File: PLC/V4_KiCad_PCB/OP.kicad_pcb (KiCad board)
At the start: 2 copper layers, 208 x 80 mm, 307 parts, among them J1 MSTBVA-2.5-10-5.08, J10 01x03_fem, J11 01x02_fem, J12 01x15_fem, J13 01x03_fem, J14 01x15_fem, J15 01x04_fem, J16 MSTBVA-2.5-10-5.08, J17 MSTBVA-2.5-10-5.08, J2 MSTBVA-2.5-10-5.08, J25 01x05_fem, J27 Lötauge, J28 GND_CAN opt an J33, J3 PFS 2x4, J33 opt. GND_XXX, J37 Lötauge, J4 01x08_fem, J40 Extention, J41 Lötauge, J42 Lötauge, J43 Flachstecker, J44 Lötauge, J45 Lötauge, J46 Lötauge, J47 Lötauge, J48 Lötauge, J5 01x04_fem, J51 Lötauge, J52 Lötauge, J6 DIN-5, J61 Lötauge, J62 Lötauge, J7 DIN-5, J8 02x02_fem, J9 Ub 0V PE, P1 1,0K lin, P2 1,0K lin, Q1 IRLML 2244, SW1 SW_DIP_x02, SW2 SW_DIP_x02, SW3 SW_DIP_x02, U1 LTV-844, U10 ADM2483xRW, U2 LTV-844, U3 LTV-844, U36 MCP3204, U39 ADuM1401xRW, U4 LTV-844, U40 ADM-803R, U42 LM4040 AIM3-2.5, U43 LM4040 AIM3-2.5, U47 ADM-809Z, U48 ADM-803L, U49 74AHC1G32, U5 MCP23S17, U50 NE555DRG4, U6 ISO1050, U7 Teensy4.0, U8 ISO1050, U9 25LC512

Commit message: OP routing optimized
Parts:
- R163, R165: moved to F.Cu
- moved R163 22.2 mm to (86.6, 76.6), turned to 0 degrees
- moved R165 19.3 mm to (86.6, 78.3), turned to 0 degrees
- moved C10 1.98 mm to (89.6, 78.0)
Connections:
- D44 pad 2: Net-(D44-Pad2) -> /RS485_B
- D45 pad 1: Net-(D44-Pad2) -> /RS485_B
- D46 pad 2: Net-(D46-Pad2) -> /RS485_A
- D47 pad 1: Net-(D46-Pad2) -> /RS485_A
- R163 pad 2: Net-(D46-Pad2) -> Net-(R163-Pad2)
- R165 pad 2: Net-(D44-Pad2) -> Net-(R165-Pad2)
- U10 pad 12: Net-(D46-Pad2) -> Net-(R163-Pad2)
- U10 pad 13: Net-(D44-Pad2) -> Net-(R165-Pad2)
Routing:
- net Net-(D44-Pad2): track 36.7 -> 0.00 mm, vias 3 -> 0
- net Net-(D46-Pad2): track 31.8 -> 0.00 mm, vias 1 -> 0
- net /RS485_B: track 29.5 -> 59.9 mm, vias 3 -> 4
- net /RS485_A: track 34.1 -> 61.2 mm, vias 2 -> 3
- net Net-(R165-Pad2): track 0.00 -> 2.94 mm
- net Net-(R163-Pad2): track 0.00 -> 2.78 mm
- net /GND_RS485_BUS: track 66.5 -> 65.9 mm
- net GNDD: vias 152 -> 157

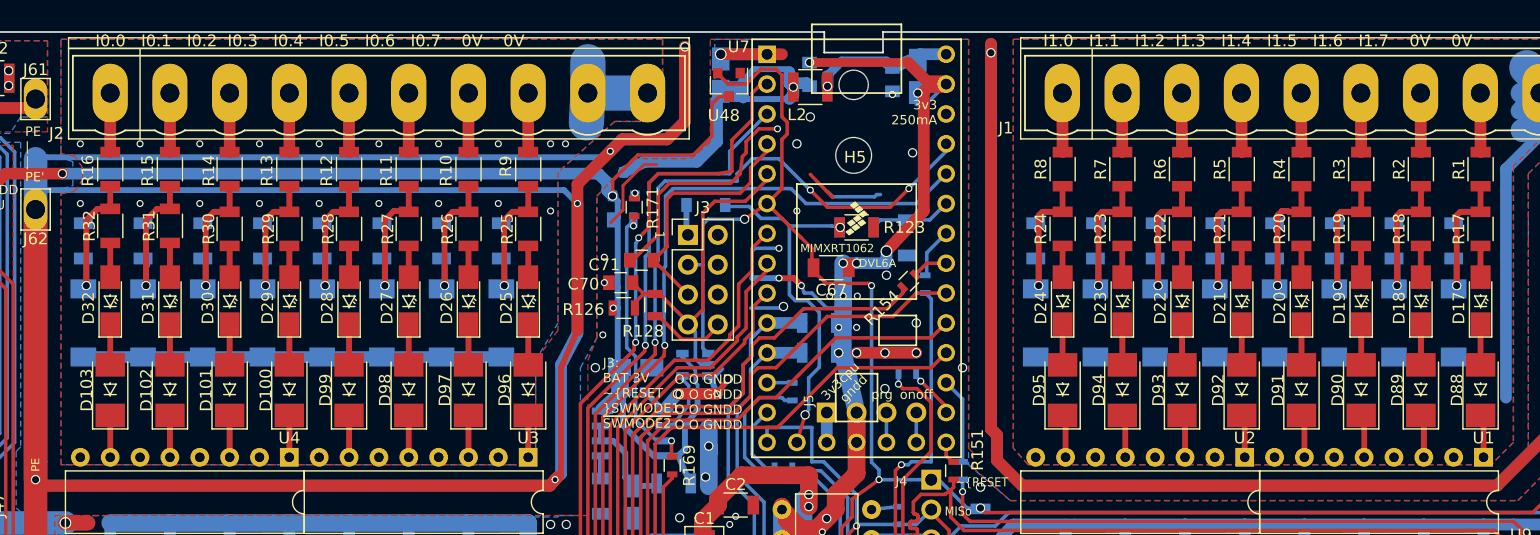
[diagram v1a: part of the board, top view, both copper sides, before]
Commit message: OP PCB mods CPU
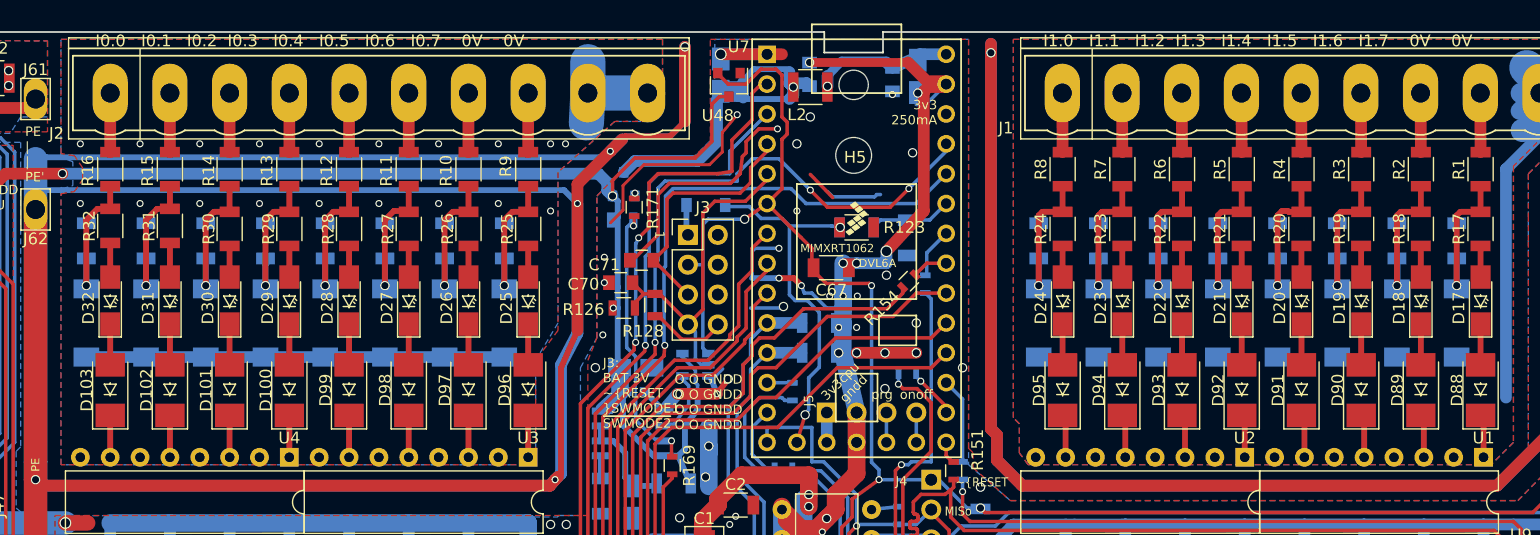
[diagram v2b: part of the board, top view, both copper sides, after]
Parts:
- moved C53 0.25 mm to (222.6, 57.8)
- moved C55 0.25 mm to (212.5, 57.8)
- moved C57 0.25 mm to (202.3, 57.8)
- moved C60 0.25 mm to (146.7, 57.8)
- moved C62 0.25 mm to (136.5, 57.8)
- moved D10 0.25 mm to (146.7, 64.8)
- moved D12 0.25 mm to (136.5, 64.8)
- moved D2 0.25 mm to (227.7, 64.8)
- moved D7 0.25 mm to (202.3, 64.8)
- moved C64 0.25 mm to (126.4, 57.8)
- moved C65 0.25 mm to (121.3, 57.8)
- moved C66 0.25 mm to (116.2, 57.8)
- moved D14 0.25 mm to (126.4, 64.8)
- moved D15 0.25 mm to (121.3, 64.8)
- moved D16 0.25 mm to (116.2, 64.8)
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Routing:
- net GNDD: track 689.0 -> 698.6 mm, vias 157 -> 158

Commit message: Kaltstart Überarbeitung
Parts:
- removed R50: 10k, Resistors_SMD:R_1206
- removed U40: ADM-803R, TO_SOT_Packages_SMD:SOT-23
- added C99: 100n, Capacitors_SMD:C_1206, F.Cu at (243.5, 76.6)
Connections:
- net /5V_CPU renamed Net-(C50-Pad1)
- net /COLDSTART_3V3INT renamed /3V3EN_Q2_UP
- C24 pad 2: /3V3_INTERFACE -> /3V3_INT
- C4 pad 1: /3V3_INTERFACE -> /3V3_INT
- C7 pad 2: /3V3_INTERFACE -> /3V3_INT
- C8 pad 1: /3V3_INTERFACE -> /3V3_INT
- D41 pad 2: /3V3_INTERFACE -> /3V3_INT
- J25 pad 1: /3V3_INTERFACE -> /3V3_INT
- J51 pad 1: /3V3_INTERFACE -> /3V3_INT
- R118 pad 2: /3V3_INTERFACE -> /3V3_INT
- U10 pad 1: /3V3_INTERFACE -> /3V3_INT
- U39 pad 1: /3V3_INTERFACE -> /3V3_INT
- U47 pad 3: /3V3_INTERFACE -> /3V3_INT
- U6 pad 1: /3V3_INTERFACE -> /3V3_INT
- U8 pad 1: /3V3_INTERFACE -> /3V3_INT
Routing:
- net /3V3_INTERFACE: track 154.1 -> 0.00 mm, vias 10 -> 0
- net /3V3_INT: track 217.4 -> 370.6 mm, vias 7 -> 17
- net GNDD: track 698.6 -> 696.9 mm, vias 158 -> 160

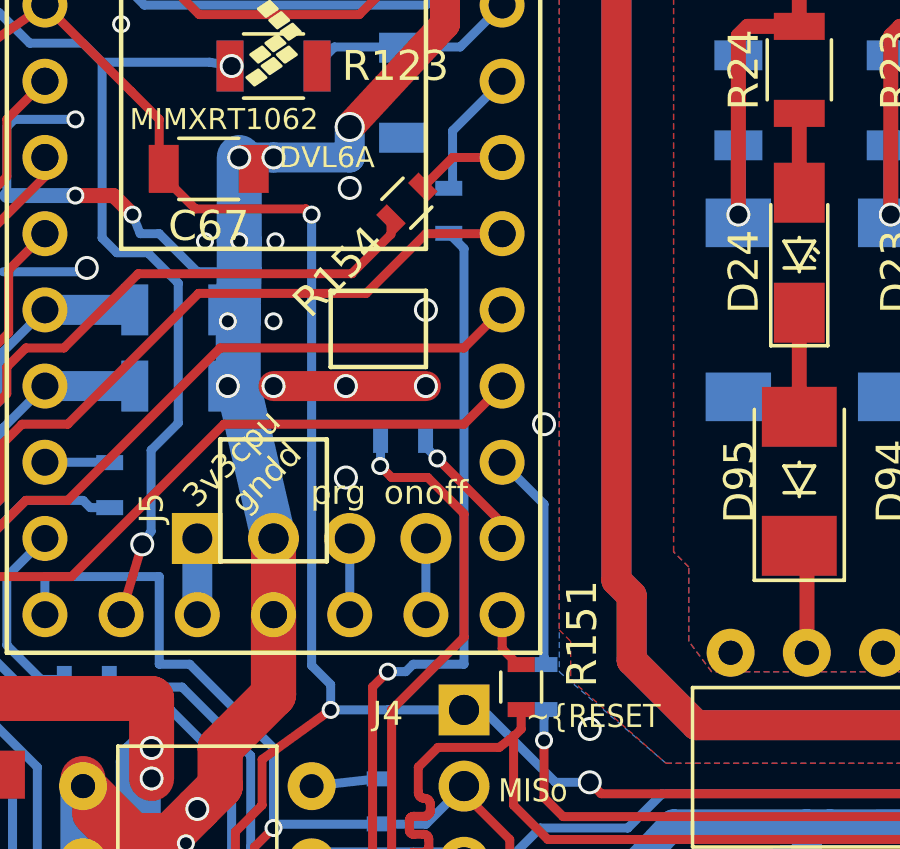
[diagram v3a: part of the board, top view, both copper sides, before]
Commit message: Überarbeitung 4-Layer-Layout und Dokumentation
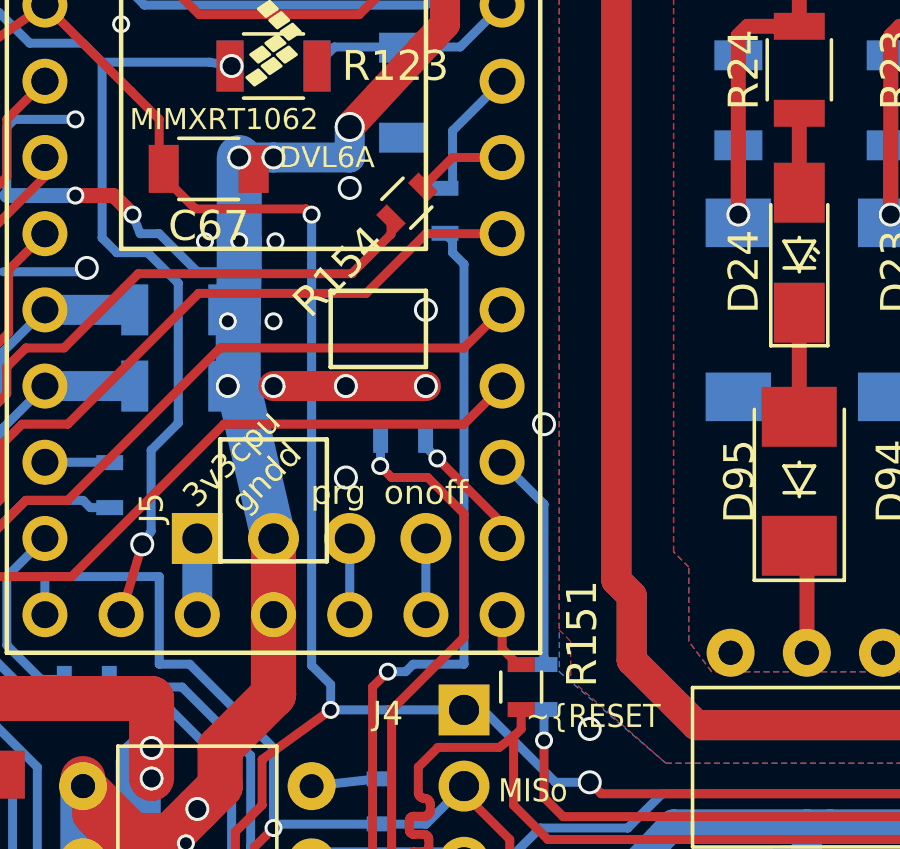
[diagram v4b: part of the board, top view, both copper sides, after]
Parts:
- moved R155 0.13 mm to (187.5, 61.5)

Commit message: V2.6 R38 final PFS
M38 final Version for PFS variant
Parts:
- added R501: 10k, Resistors_SMD:R_1206, F.Cu at (245.0, 76.7)
- moved C99 0.83 mm to (242.7, 76.6)
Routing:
- net GNDD: track 696.9 -> 692.7 mm
- net /PE: track 1070.4 -> 1068.7 mm
- net /~EE_HOLD: vias 3 -> 2
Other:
- board text added: "PE PE 3V3 (7) (11) ~RES ~CS SO CK SI GNDD"
- board text added: "PFS CPU Board V2.6 M38 2024-01-17"
- board text removed: "PE PE 3V3 (7) GNDD (11) ~RES ~CS SO CK SI GNDD"
- board text removed: "PFS CPU Board V2.6 M37 2023-11-23"

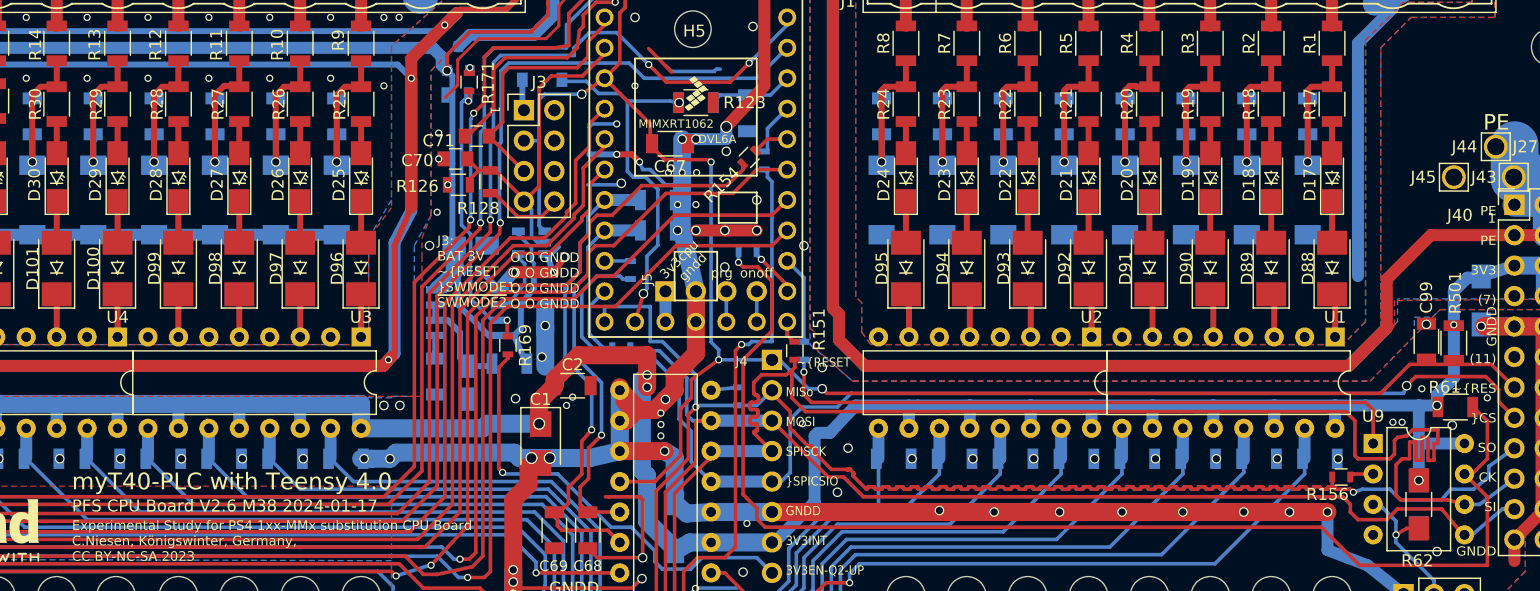
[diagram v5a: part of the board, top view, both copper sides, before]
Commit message: V2.8 M40 Coldstart Issues
Coldstart issues, some PullUps to high dimensioned, no high logic resulting together with switched-off Teensy and its input impedances.
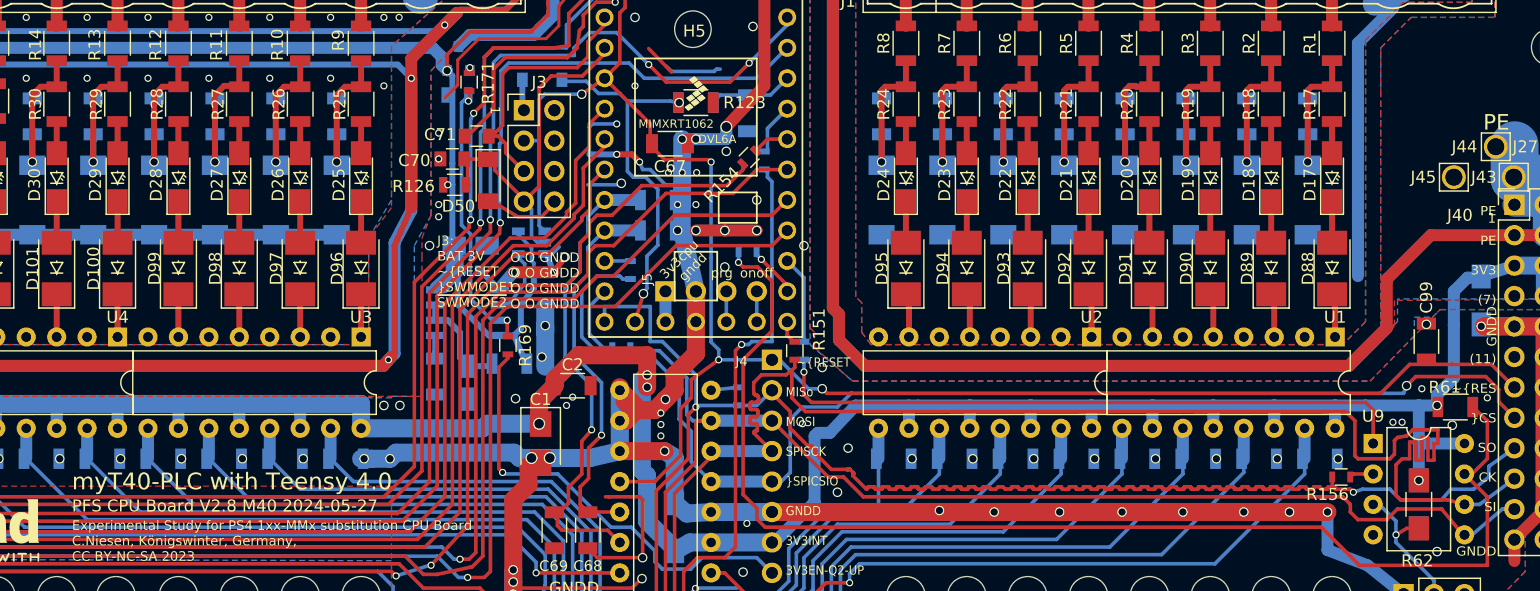
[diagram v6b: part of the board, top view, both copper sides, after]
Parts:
- removed R128: 16k, Resistors_SMD:R_0805
- removed R501: 10k, Resistors_SMD:R_1206
- added D50: 3V0, Diodes_SMD:D_MiniMELF, F.Cu at (164.4, 63.1)
- R126: value 10k -> 2k7
- moved R126 0.32 mm to (161.6, 63.5)
- moved C70 0.25 mm to (161.4, 61.3)
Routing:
- net /~SW_MODE_2: track 29.1 -> 30.8 mm
- net /~SW_MODE_1: track 21.7 -> 22.3 mm
- net GNDD: track 692.7 -> 692.1 mm, vias 160 -> 161
- net /3V3_INT: vias 17 -> 16
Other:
- board text added: "PFS CPU Board V2.8 M40 2024-05-27"
- board text removed: "PFS CPU Board V2.6 M38 2024-01-17"
